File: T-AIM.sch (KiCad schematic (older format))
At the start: 44 parts, among them IC1 ATMEGA328PB-A, IC2 MAX17043, J1 ADXL345 Connector, J2 PIR Sensor Connector, J3 JY-MCU HC-05 Pins, SW1 Connection Button, SW2 Reset Button, U1 TPS61200

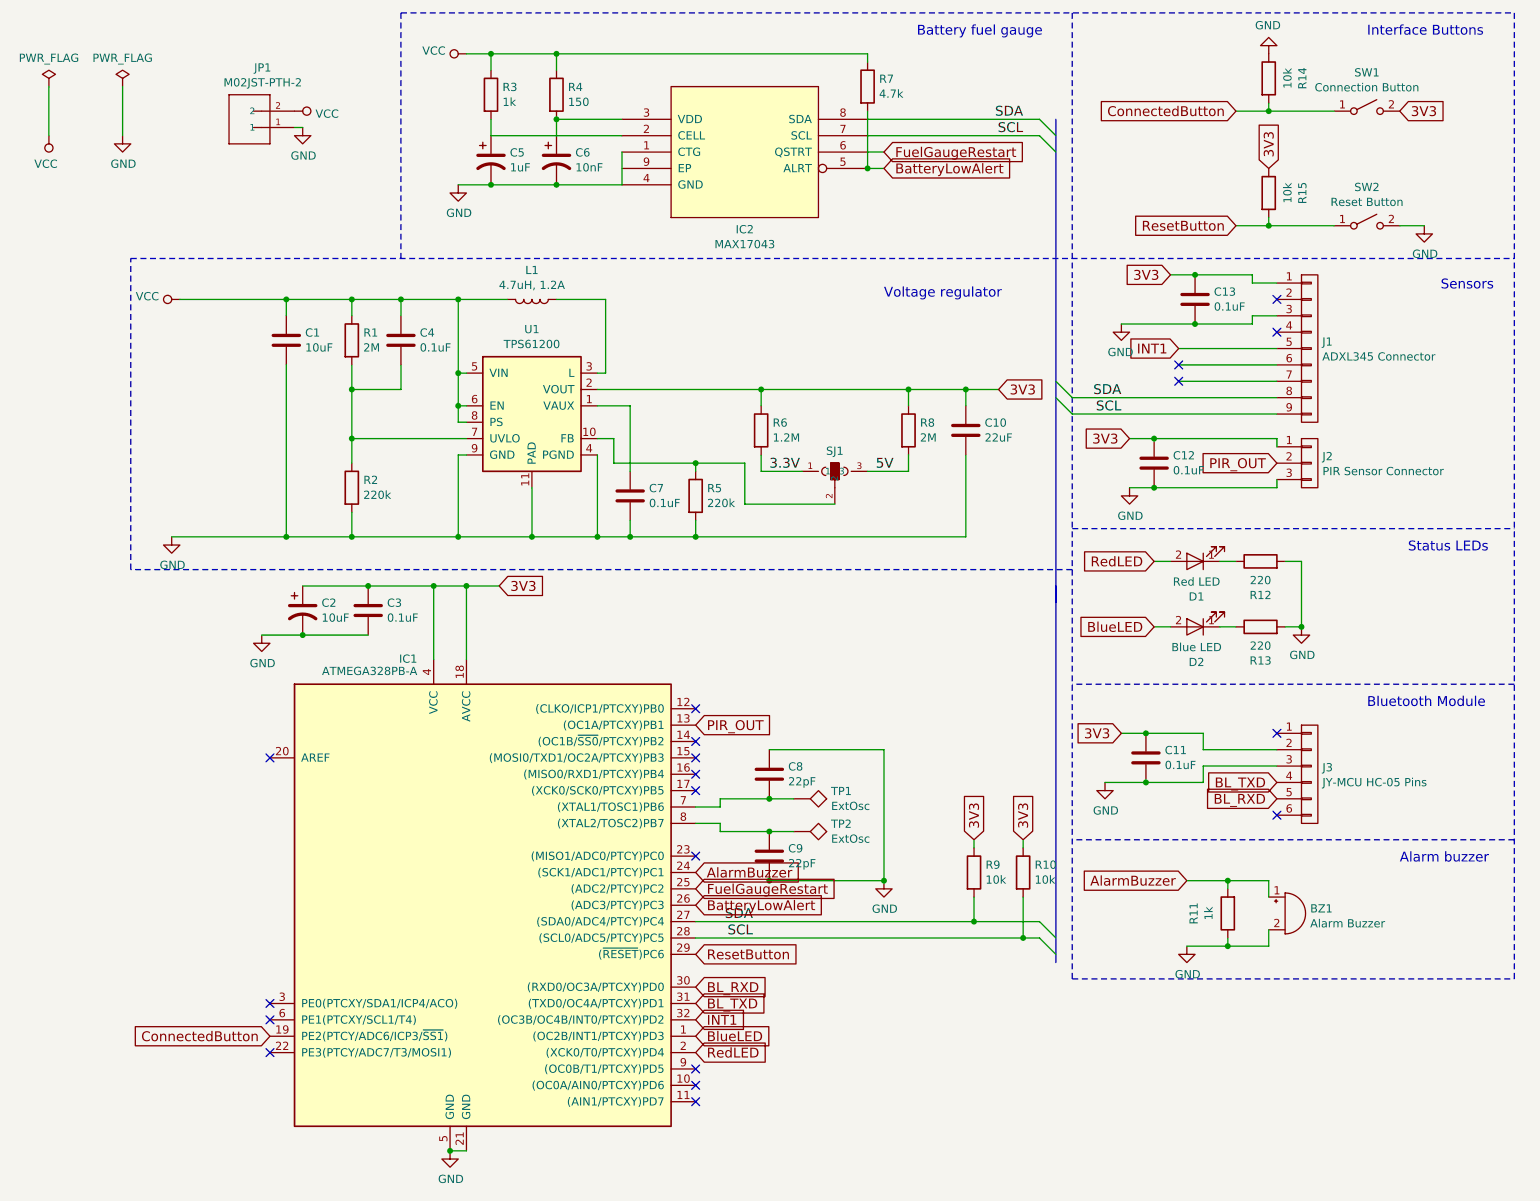
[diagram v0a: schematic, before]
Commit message: Components placed to layout
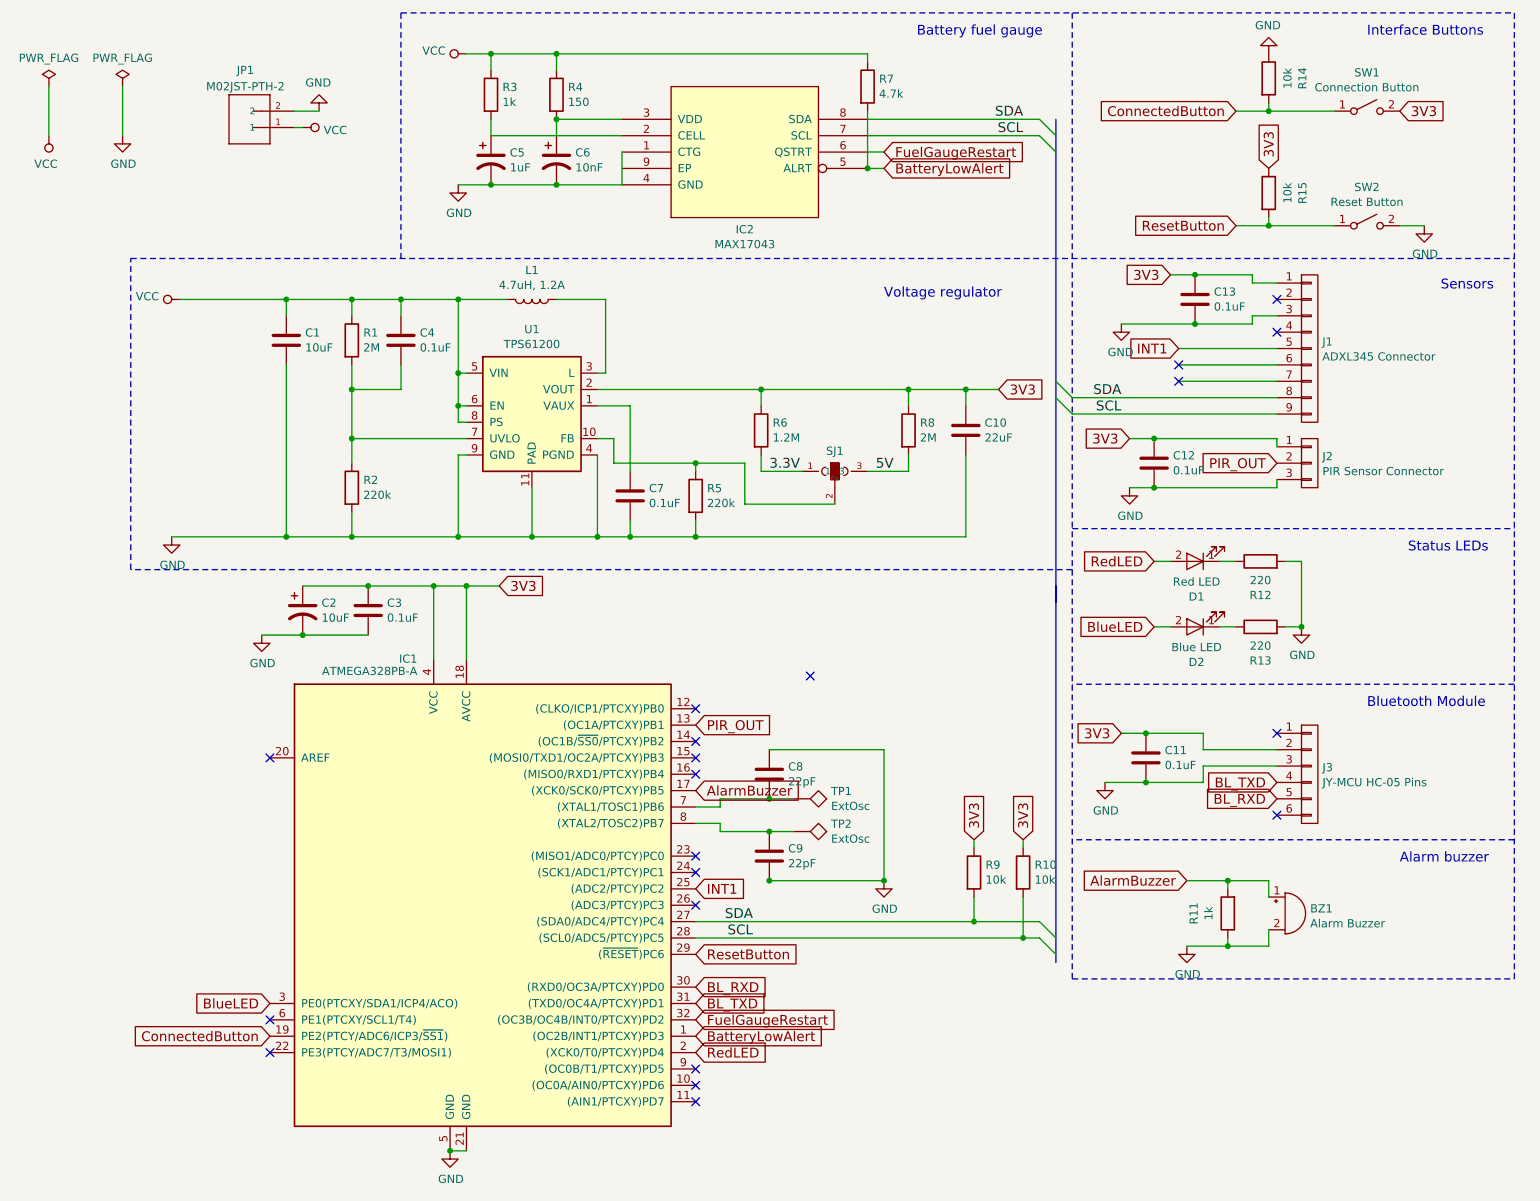
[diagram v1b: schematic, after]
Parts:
- J3: footprint Pin_Headers:Pin_Header_Straight_1x06_Pitch2.54mm -> Pin_Headers:Pin_Header_Straight_1x06_Pitch2.00mm
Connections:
- net AlarmBuzzer: now also IC1.17 ((XCK0/SCK0/PTCXY)PB5); no longer IC1.24 ((SCK1/ADC1/PTCY)PC1)
- net BatteryLowAlert: now also IC1.1 ((OC2B/INT1/PTCXY)PD3); no longer IC1.26 ((ADC3/PTCY)PC3)
- net BlueLED: now also IC1.3 (PE0(PTCXY/SDA1/ICP4/ACO)); no longer IC1.1 ((OC2B/INT1/PTCXY)PD3)
- net FuelGaugeRestart: now also IC1.32 ((OC3B/OC4B/INT0/PTCXY)PD2); no longer IC1.25 ((ADC2/PTCY)PC2)
- net GND: now also JP1.2; no longer JP1.1
- net INT1: now also IC1.25 ((ADC2/PTCY)PC2); no longer IC1.32 ((OC3B/OC4B/INT0/PTCXY)PD2)
- net VCC: now also JP1.1; no longer JP1.2
- no-connect marks 19 -> 20
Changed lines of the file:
@@
 Text GLabel 4850 6950 2    60   Input ~ 0
 RedLED
-Text GLabel 4850 6850 2    60   Input ~ 0
+Text GLabel 2250 6650 0    60   Input ~ 0
 BlueLED
 $Comp
@@
 Text GLabel 7650 4350 0    60   Input ~ 0
 BlueLED
-Text GLabel 4850 5850 2    60   Input ~ 0
+Text GLabel 4850 5350 2    60   Input ~ 0
 AlarmBuzzer
 Text GLabel 7850 5900 0    60   Input ~ 0
@@
 F 0 "J3" H 8678 5291 50  0000 L CNN
 F 1 "JY-MCU HC-05 Pins" H 8678 5200 50  0000 L CNN
-F 2 "Pin_Headers:Pin_Header_Straight_1x06_Pitch2.54mm" H -650 1350 50  0001 C CNN
-F 3 "" H -650 1350 50  0001 C CNN
+F 2 "Pin_Headers:Pin_Header_Straight_1x06_Pitch2.00mm" H -650 1350 50  0001 C CNN
+F 3 "http://www.electronica60norte.com/mwfls/pdf/newBluetooth.pdf" H -650 1350 50  0001 C CNN
 	1    8600 5250
 	1    0    0    -1
@@
 	1    0    0    -1
 $EndComp
-NoConn ~ 2250 6650
 NoConn ~ 2250 6750
 $Comp
@@
 U 1 1 58CB4869
 P 2100 1300
-F 0 "JP1" H 2206 1665 50  0000 C CNN
-F 1 "M02JST-PTH-2" H 2206 1574 50  0000 C CNN
+F 0 "JP1" H 2100 1650 50  0000 C CNN
+F 1 "M02JST-PTH-2" H 2100 1550 50  0000 C CNN
 F 2 "SparkFun-Connectors:JST-2-PTH" H -10800 -2200 50  0001 C CNN
 F 3 "" H -10800 -2350 60  0001 C CNN
@@
 	1    0    0    -1
 $EndComp
-NoConn ~ 4850 5350
 NoConn ~ 8400 5500
 NoConn ~ 4850 5050
@@
 	-1   0    0    1
 $EndComp
-Text GLabel 4850 5950 2    60   Input ~ 0
+Text GLabel 4850 6750 2    60   Input ~ 0
 FuelGaugeRestart
-Text GLabel 4850 6050 2    60   Input ~ 0
+Text GLabel 4850 6850 2    60   Input ~ 0
 BatteryLowAlert
 $Comp
 L VCC #PWR05
 U 1 1 58CB4999
-P 2400 1200
-F 0 "#PWR05" H 1350 -700 50  0001 C CNN
-F 1 "VCC" V 2417 1328 50  0000 L CNN
-F 2 "" H 1350 -550 50  0001 C CNN
-F 3 "" H 1350 -550 50  0001 C CNN
-	1    2400 1200
+P 2450 1300
+F 0 "#PWR05" H 1400 -600 50  0001 C CNN
+F 1 "VCC" V 2467 1428 50  0000 L CNN
+F 2 "" H 1400 -450 50  0001 C CNN
+F 3 "" H 1400 -450 50  0001 C CNN
+	1    2450 1300
 	0    1    1    0
 $EndComp
@@
 L GND #PWR06
 U 1 1 58CB499F
-P 2450 1300
-F 0 "#PWR06" H 400 0   50  0001 C CNN
-F 1 "GND" H 2455 1127 50  0000 C CNN
-F 2 "" H 400 250 50  0001 C CNN
-F 3 "" H 400 250 50  0001 C CNN
-	1    2450 1300
-	1    0    0    -1
+P 2550 1200
+F 0 "#PWR06" H 500 -100 50  0001 C CNN
+F 1 "GND" H 2555 1027 50  0000 C CNN
+F 2 "" H 500 150 50  0001 C CNN
+F 3 "" H 500 150 50  0001 C CNN
+	1    2550 1200
+	-1   0    0    1
 $EndComp
 $Comp
@@
 NoConn ~ 7800 2850
 NoConn ~ 7800 2750
-Text GLabel 4850 6750 2    60   Input ~ 0
+Text GLabel 4850 5950 2    60   Input ~ 0
 INT1
 $Comp
@@
 Connection ~ 7600 5300
 Wire Wire Line
-	2400 1300 2450 1300
+	2400 1200 2550 1200
 Wire Wire Line
 	2750 3650 2750 3800
@@
 NoConn ~ 4850 7050
 NoConn ~ 4850 4850
+Wire Wire Line
+	2450 1300 2400 1300
+NoConn ~ 4850 5850
+NoConn ~ 5550 4650
+NoConn ~ 4850 6050
 $EndSCHEMATC

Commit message: Test text added
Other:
- note added: "3.7V"
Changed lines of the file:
@@
 NoConn ~ 5550 4650
 NoConn ~ 4850 6050
+Text Notes 1450 5100 0    60   ~ 0
+3.7V
 $EndSCHEMATC

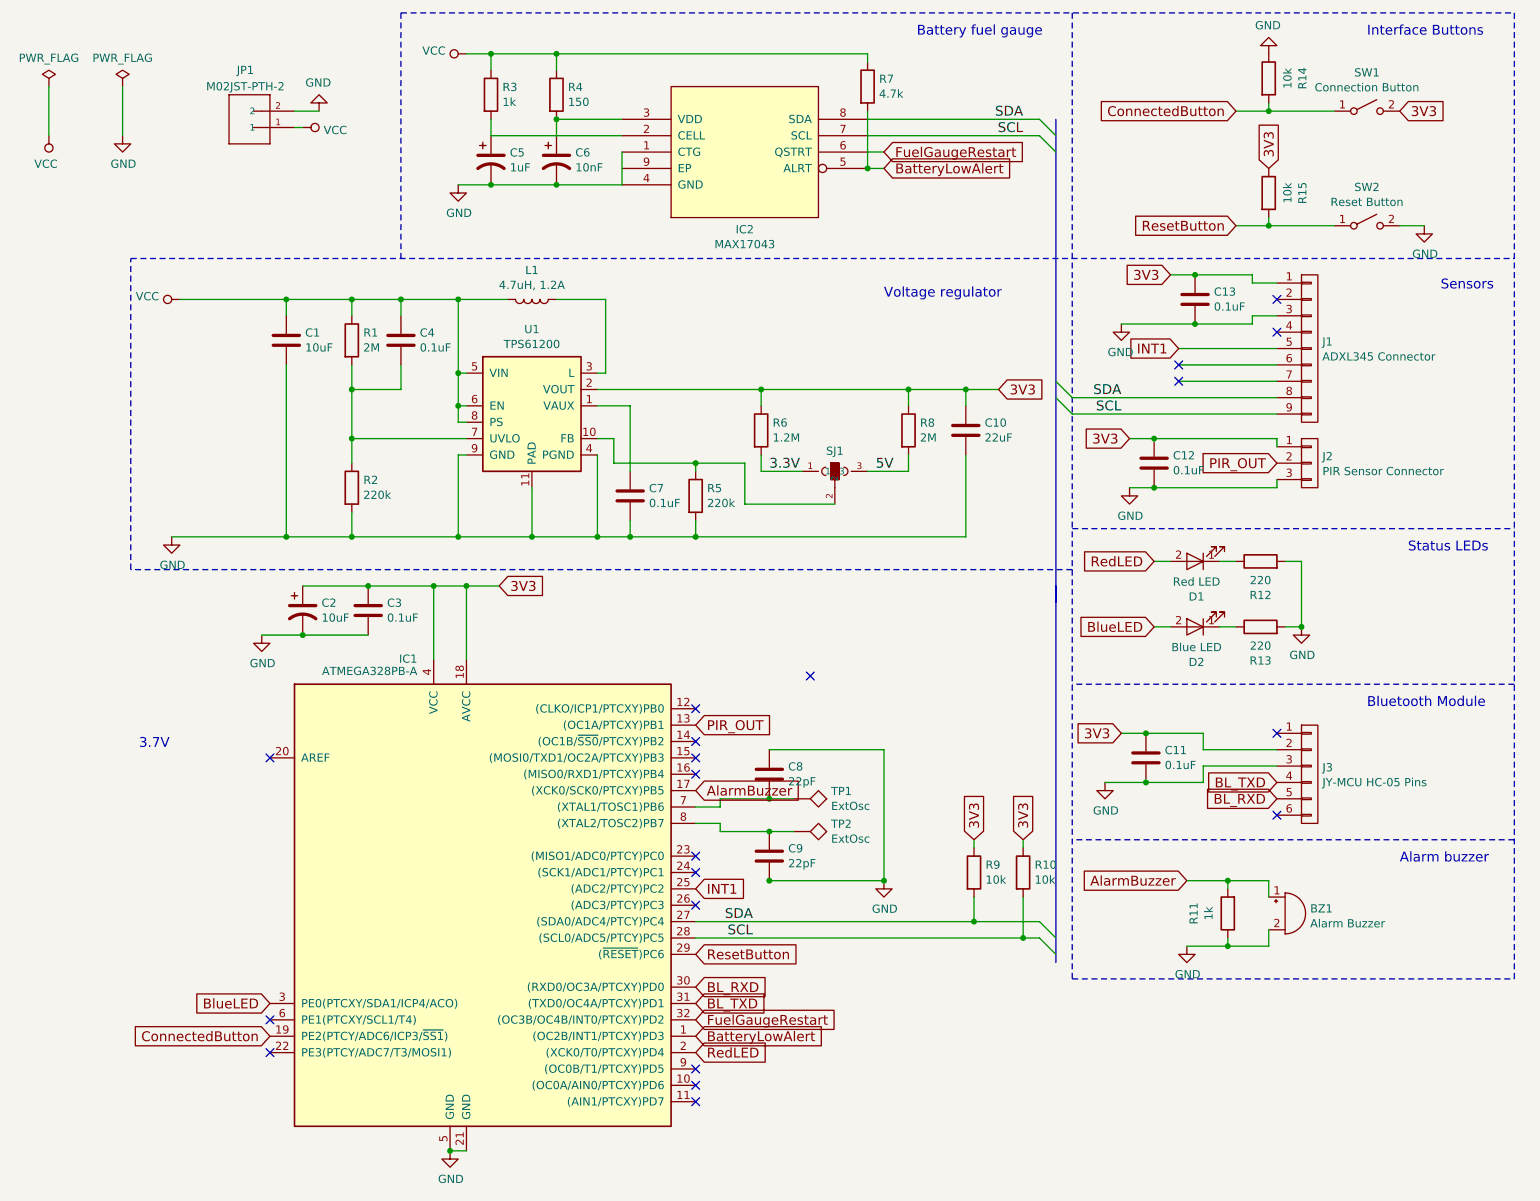
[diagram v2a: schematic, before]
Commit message: Schematic updated for 3.7V; Changed Buzzer resistor to 1M; PCB updated for SF LiPo Gauge; Gerbers generated
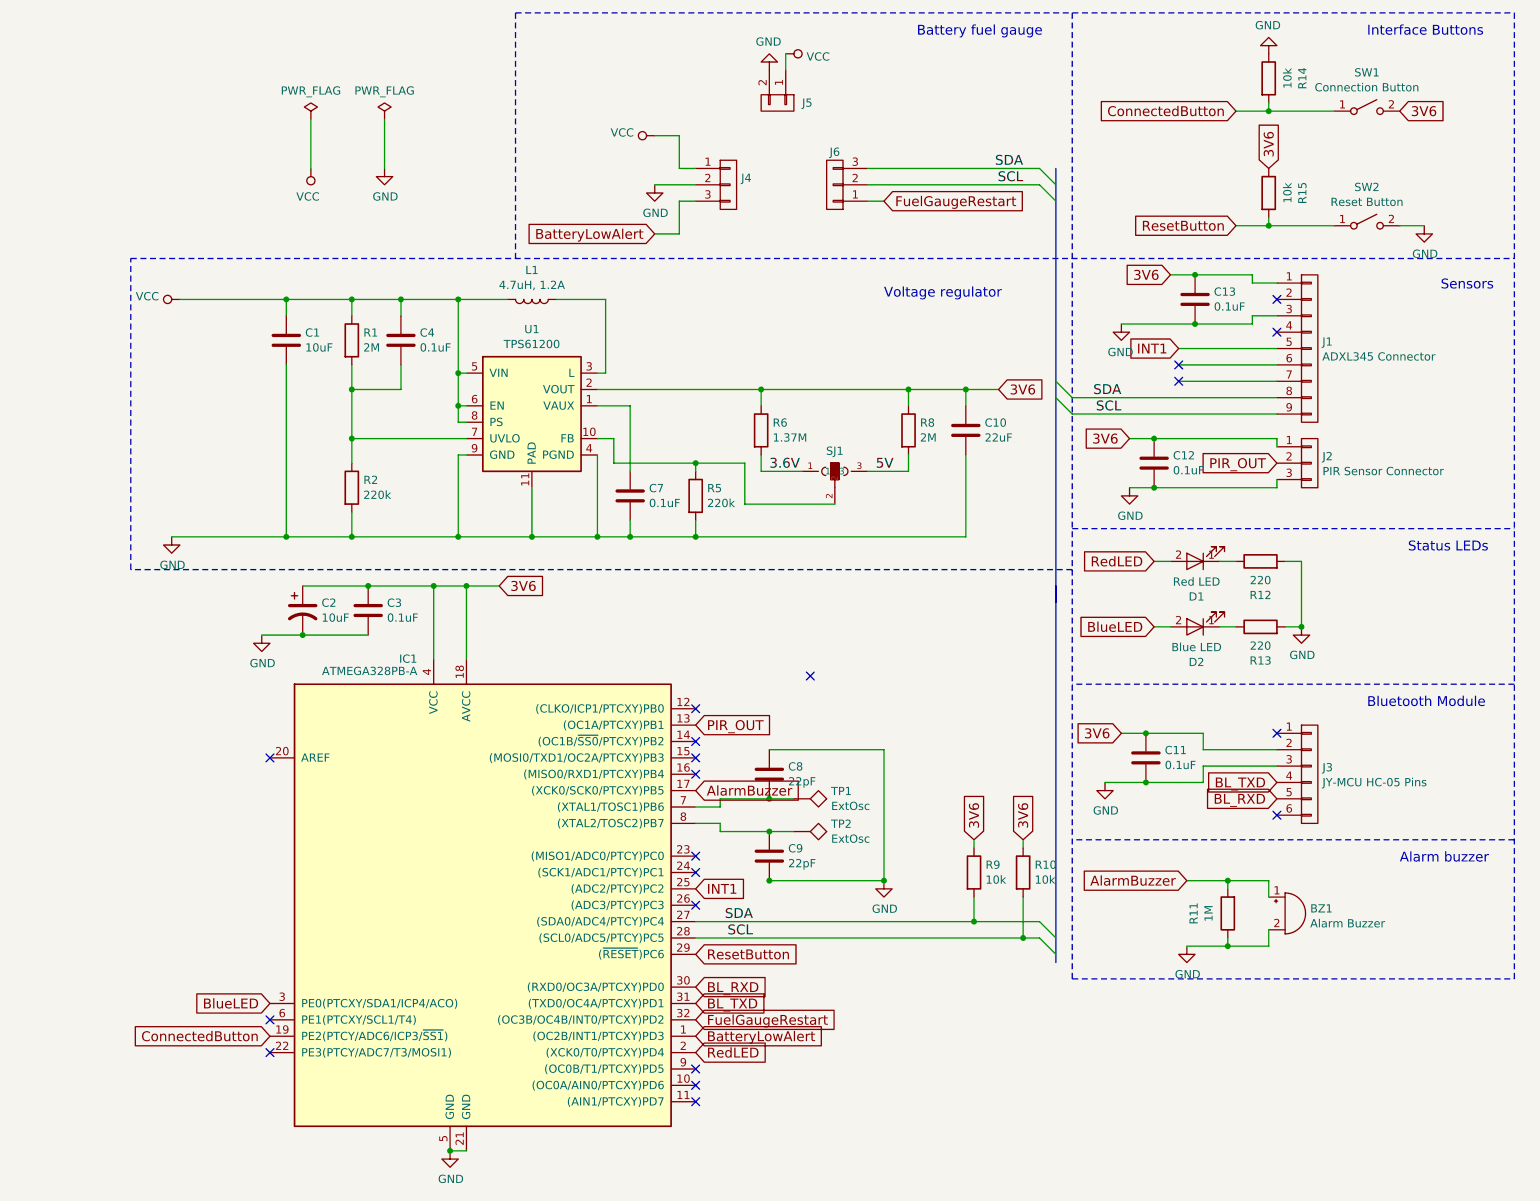
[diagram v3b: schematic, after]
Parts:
- removed C5: 1uF, Capacitors_SMD:CP_Elec_5x5.3, symbol CP1
- removed C6: 10nF, Capacitors_SMD:CP_Elec_5x5.3, symbol CP1
- removed IC2: MAX17043, SparkFun-PowerIC:TDFN-8, symbol MAX17043
- removed JP1: M02JST-PTH-2, SparkFun-Connectors:JST-2-PTH, symbol M02JST-PTH-2
- removed R3: 1k, Resistors_SMD:R_0805_HandSoldering, symbol R
- removed R4: 150, Resistors_SMD:R_0805_HandSoldering, symbol R
- removed R7: 4.7k, Resistors_SMD:R_0805_HandSoldering, symbol R
- added J4, J6: CONN_01X03, Pin_Headers:Pin_Header_Straight_1x03_Pitch2.54mm, symbol CONN_01X03
- added J5: CONN_01X02, Pin_Headers:Pin_Header_Straight_1x02_Pitch2.54mm, symbol CONN_01X02
- R11: value 1k -> 1M
- R6: value 1.2M -> 1.37M
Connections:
- net BatteryLowAlert: now also J4.3 (P3)
- net FuelGaugeRestart: now also J6.1 (P1)
- net GND: now also J4.2 (P2), J5.2 (P2)
- net SCL: now also J6.2 (P2)
- net SDA: now also J6.3 (P3)
- net VCC: now also J4.1 (P1), J5.1 (P1)
- net 3.3V renamed 3.6V
- net 3V3 renamed 3V6
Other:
- note removed: "3.7V"

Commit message: Updated TPS61200 Thermal Pad, PCB Layout and Gerbers; Slightly edited schematics
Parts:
- U1: footprint SparkFun-PowerIC:DRC-10 -> T-AIM:DRC-10-Thermal-Vias
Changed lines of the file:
@@
 LIBS:SparkFun
 LIBS:maxium
+LIBS:T-AIMCOMPS
 LIBS:T-AIM-cache
 EELAYER 26 0
@@
 NoConn ~ 2250 6750
 $Comp
-L TPS61200 U1
-U 1 1 58CB485B
-P 3850 3000
-F 0 "U1" H 3850 3467 50  0000 C CNN
-F 1 "TPS61200" H 3850 3376 50  0000 C CNN
-F 2 "SparkFun-PowerIC:DRC-10" H -11300 -800 50  0001 L CNN
-F 3 "https://www.sparkfun.com/datasheets/Prototyping/tps61200.pdf" H -11350 -350 50  0001 C CNN
-	1    3850 3000
-	1    0    0    -1
-$EndComp
-$Comp
 L L L1
 U 1 1 58CB4862
@@
 Wire Wire Line
 	5400 850  5400 950
+$Comp
+L TPS61200 U1
+U 1 1 58DE14EE
+P 3850 3000
+F 0 "U1" H 3850 3467 50  0000 C CNN
+F 1 "TPS61200" H 3850 3376 50  0000 C CNN
+F 2 "T-AIM:DRC-10-Thermal-Vias" H 2250 -650 50  0001 L CNN
+F 3 "" H 2200 -200 50  0001 C CNN
+	1    3850 3000
+	1    0    0    -1
+$EndComp
 $EndSCHEMATC
